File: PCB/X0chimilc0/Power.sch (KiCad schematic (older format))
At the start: 0 parts

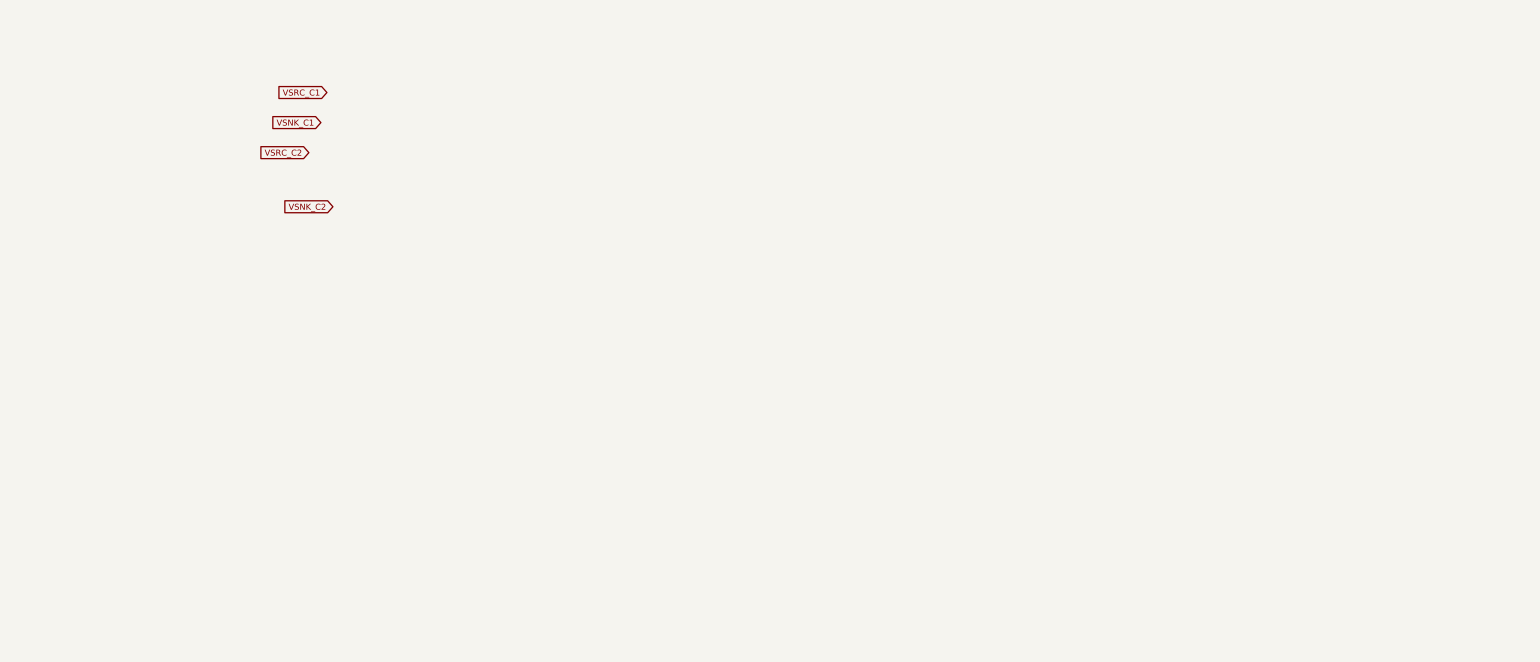
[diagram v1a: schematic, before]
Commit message: Power Supply
Worked on power supply design adn schematic, still need a few more rails.
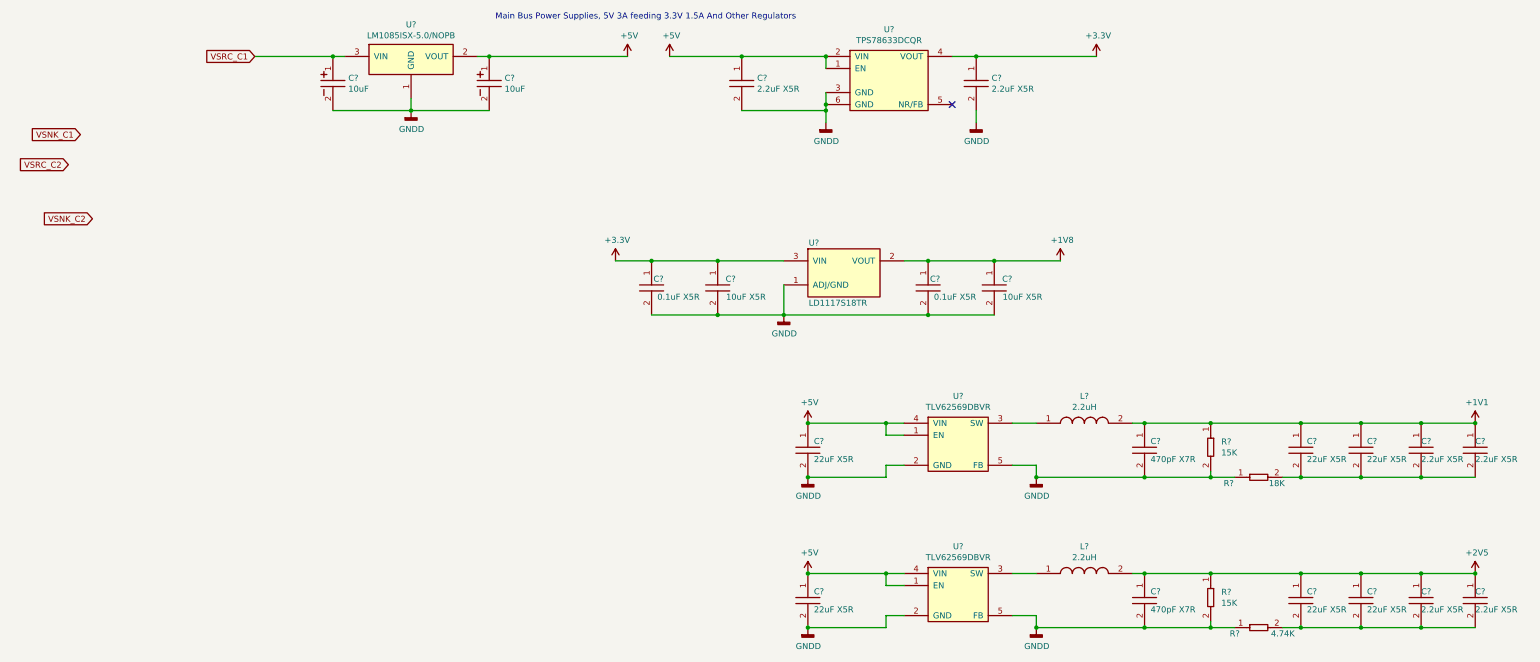
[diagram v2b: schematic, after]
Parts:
- added C? (x6): CC0603KRX5R6BB225, AVR-KiCAD-Lib-Capacitors:C0603, symbol AVR-KiCAD-Lib-Capacitors:CC0603KRX5R6BB225
- added C? (x2): T491A106K010AT, AVR-KiCAD-Lib-Capacitors:CP_Tantalum_Case-A_EIA-3216-18_Reflow, symbol AVR-KiCAD-Lib-Capacitors:T491A106K010AT
- added C? (x2): GRM188R61A106KE69D, AVR-KiCAD-Lib-Capacitors:C0603, symbol AVR-KiCAD-Lib-Capacitors:GRM188R61A106KE69D
- added C? (x2): C0402C104K9PACTU, AVR-KiCAD-Lib-Resistors:R0402, symbol AVR-KiCAD-Lib-Capacitors:C0402C104K9PACTU
- added C? (x2): CC0603KRX7R9BB471, AVR-KiCAD-Lib-Capacitors:C0603, symbol AVR-KiCAD-Lib-Capacitors:CC0603KRX7R9BB471
- added C? (x6): GRM21BR61A226ME51L, AVR-KiCAD-Lib-Capacitors:C0805, symbol AVR-KiCAD-Lib-Capacitors:GRM21BR61A226ME51L
- added L? (x2): L1210R2R2MDWIT, AVR-KiCAD-Lib-Inductors:I1210, symbol AVR-KiCAD-Lib-Inductors:L1210R2R2MDWIT
- added R?: RC0603FR-074K7P, AVR-KiCAD-Lib-Resistors:R0603, symbol AVR-KiCAD-Lib-Resistors:RC0603FR-074K7P
- added R? (x2): RC0603FR-0715KL, AVR-KiCAD-Lib-Resistors:R0603, symbol AVR-KiCAD-Lib-Resistors:RC0603FR-0715KL
- added R?: RC0603FR-0718KL, AVR-KiCAD-Lib-Resistors:R0603, symbol AVR-KiCAD-Lib-Resistors:RC0603FR-0718KL
- added U?: LM1085ISX-5.0_NOPB, AVR-KiCAD-Lib-ICs:LM1085ISX-5.0_NOPB, symbol AVR-KiCAD-Lib-ICs:LM1085ISX-5.0_NOPB
- added U?: TPS78633DCQR, AVR-KiCAD-Lib-ICs:SOT-223-6, symbol AVR-KiCAD-Lib-ICs:TPS78633DCQR
- added U?: LD1117S18TR, AVR-KiCAD-Lib-ICs:LD1117S50TR, symbol AVR-KiCAD-Lib-ICs:LD1117S18TR
- added U? (x2): TLV62569DBVR, AVR-KiCAD-Lib-ICs:SOT-23-5, symbol AVR-KiCAD-Lib-ICs:TLV62569DBVR
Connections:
- net VSRC_C1: now also C?.1, U?.3 (VIN)
- new net: L?.1, U?.3 (SW) (x2)
- new net: C?.2, C?.2, C?.2, C?.2, R?.2 (x2)
- new net +1V1: C?.1, C?.1, C?.1, C?.1, C?.1, L?.2, R?.1
- new net +1V8: C?.1, C?.1, U?.2 (VOUT)
- new net +2V5: C?.1, C?.1, C?.1, C?.1, C?.1, L?.2, R?.1
- new net +3V3: C?.1, C?.1, C?.1, U?.3 (VIN), U?.4 (VOUT)
- new net +5V: C?.1, C?.1, C?.1, C?.1, U?.1 (EN), U?.1 (EN), U?.1 (EN), U?.2 (VIN), U?.2 (VOUT), U?.4 (VIN), U?.4 (VIN)
- new net GNDD: C?.2, C?.2, C?.2, C?.2, C?.2, C?.2, C?.2, C?.2, C?.2, C?.2, C?.2, C?.2, R?.1, R?.1, R?.2, R?.2, U?.1 (ADJ/GND), U?.1 (GND), U?.2 (GND), U?.2 (GND), U?.3 (GND), U?.5 (FB), U?.5 (FB), U?.6 (GND)
- no-connect marks 0 -> 1
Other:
- note added: "Main Bus Power Supplies, 5V 3A feeding 3.3V 1.5A And Other Regulators"
